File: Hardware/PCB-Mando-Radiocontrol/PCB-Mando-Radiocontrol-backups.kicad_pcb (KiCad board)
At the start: 2 copper layers, 132 x 66 mm, 25 parts, among them J1 USB 2.0 a UART TTL 6 pines CP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, J2 ALIMENTACION, SW1 SW_SPDT, SW2 SW_SPDT, SW3 SW_SPDT, U1 ATMEGA328P, U2 Nrf24l01, U3 AMS1117-3.3, U4 AMS1117-5.0, U5 COM-09032, U6 COM-09032, Y1 16MHZ

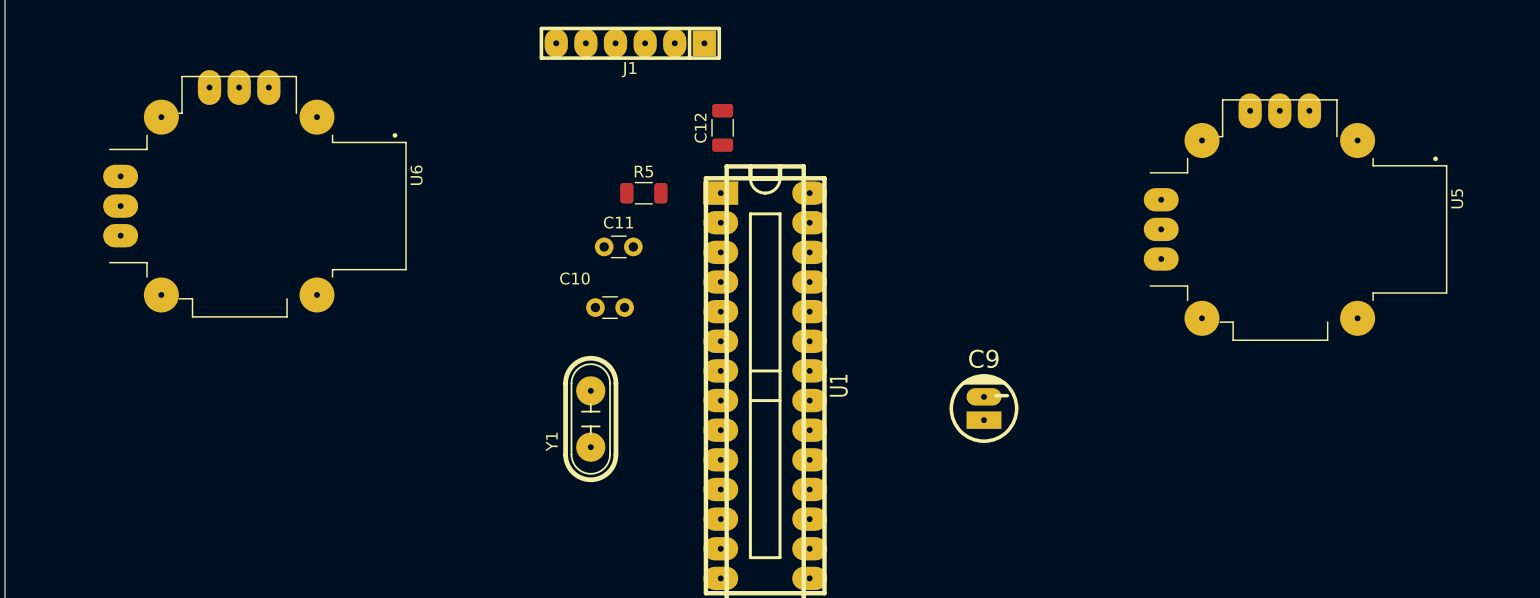
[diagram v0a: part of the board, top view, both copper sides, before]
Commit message: Reordenamiento de componentes
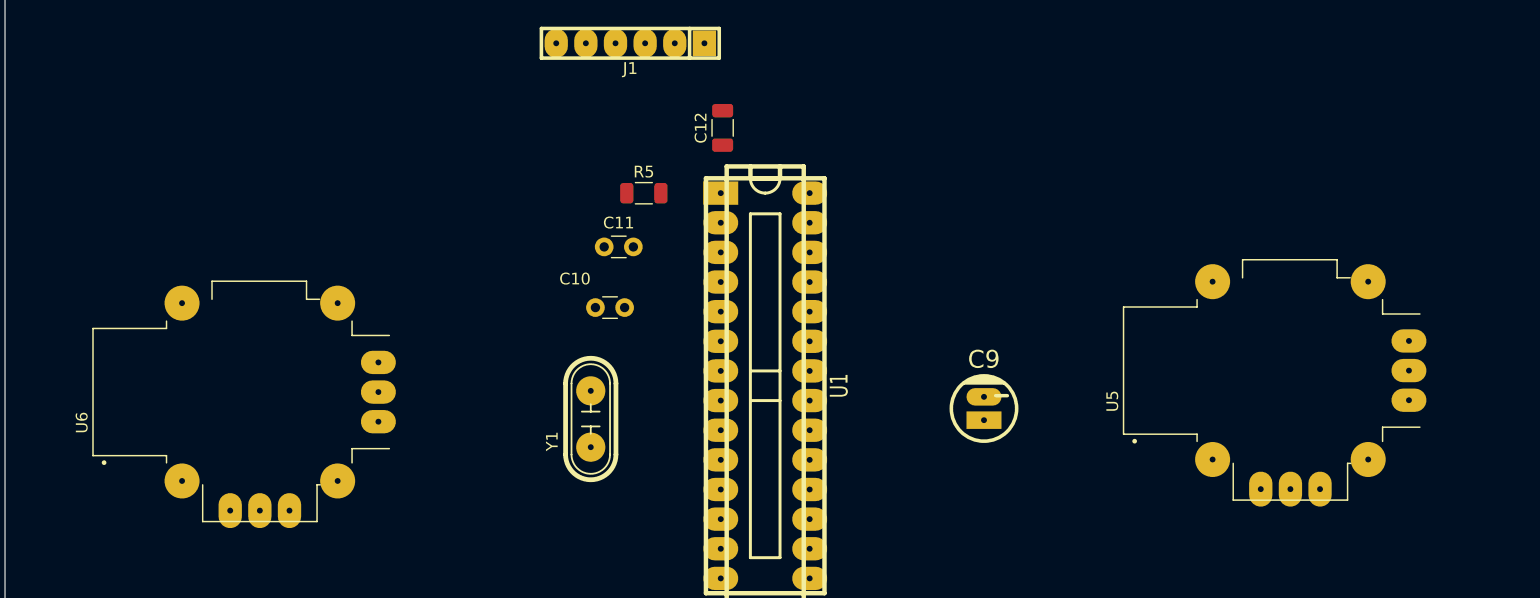
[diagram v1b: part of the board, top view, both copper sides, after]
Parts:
- moved U6 16.0 mm to (112.8, 98.8), turned to 90 degrees
- moved U5 12.1 mm to (201.2, 97.0), turned to 90 degrees
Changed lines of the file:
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@@
   )
   (footprint "PotStick:XDCR_COM-09032" (layer "F.Cu")
-    (at 111.068719 82.9 -90)
+    (at 112.84 98.84 90)
     (property "MANUFACTURER" "SparkFun Electronics")
     (property "MAXIMUM_PACKAGE_HEIGHT" "30.1mm")
@@
       (stroke (width 0.2) (type solid)) (fill none) (layer "F.Fab"))
     (dimension (type aligned) (layer "Edge.Cuts")
-      (pts (xy 117.736219 90.52) (xy 104.401219 90.52))
+      (pts (xy 106.1725 91.22) (xy 119.5075 91.22))
       (height -7.62)
-      (gr_text "13,3350 mm" (at 111.068719 96.99) (layer "Edge.Cuts")
+      (gr_text "13,3350 mm" (at 112.84 82.45) (layer "Edge.Cuts")
         (effects (font (size 1 1) (thickness 0.15)))
       )
@@
     )
     (dimension (type aligned) (layer "Edge.Cuts")
-      (pts (xy 113.608719 72.74) (xy 108.528719 72.74))
+      (pts (xy 110.3 109) (xy 115.38 109))
       (height 7.62)
-      (gr_text "5,0800 mm" (at 111.068719 63.97) (layer "Edge.Cuts")
+      (gr_text "5,0800 mm" (at 112.84 115.47) (layer "Edge.Cuts")
         (effects (font (size 1 1) (thickness 0.15)))
       )
@@
       (style (thickness 0.05) (arrow_length 1.27) (text_position_mode 0) (extension_height 0.58642) (extension_offset 0.5) keep_text_aligned)
     )
-    (pad "H1" thru_hole oval (at -2.54 10.16 270) (size 2 3) (drill 0.5) (layers "*.Cu" "*.Mask")
+    (pad "H1" thru_hole oval (at -2.54 10.16 90) (size 2 3) (drill 0.5) (layers "*.Cu" "*.Mask")
       (net 3 "+5V") (pinfunction "H+") (pintype "passive"))
-    (pad "H2" thru_hole oval (at 0 10.16 270) (size 2 3) (drill 0.5) (layers "*.Cu" "*.Mask")
+    (pad "H2" thru_hole oval (at 0 10.16 90) (size 2 3) (drill 0.5) (layers "*.Cu" "*.Mask")
       (net 27 "/PotIzqA") (pinfunction "H") (pintype "passive"))
-    (pad "H3" thru_hole oval (at 2.54 10.16 270) (size 2 3) (drill 0.5) (layers "*.Cu" "*.Mask")
+    (pad "H3" thru_hole oval (at 2.54 10.16 90) (size 2 3) (drill 0.5) (layers "*.Cu" "*.Mask")
       (net 2 "GND") (pinfunction "H-") (pintype "passive"))
-    (pad "S1" thru_hole circle (at -7.62 -6.6675 270) (size 3 3) (drill 0.5) (layers "*.Cu" "*.Mask")
+    (pad "S1" thru_hole circle (at -7.62 -6.6675 90) (size 3 3) (drill 0.5) (layers "*.Cu" "*.Mask")
       (net 2 "GND") (pinfunction "SHIELD") (pintype "passive"))
-    (pad "S2" thru_hole circle (at -7.62 6.6675 270) (size 3 3) (drill 0.5) (layers "*.Cu" "*.Mask")
+    (pad "S2" thru_hole circle (at -7.62 6.6675 90) (size 3 3) (drill 0.5) (layers "*.Cu" "*.Mask")
       (net 2 "GND") (pinfunction "SHIELD") (pintype "passive"))
-    (pad "S3" thru_hole circle (at 7.62 6.6675 270) (size 3 3) (drill 0.5) (layers "*.Cu" "*.Mask")
+    (pad "S3" thru_hole circle (at 7.62 6.6675 90) (size 3 3) (drill 0.5) (layers "*.Cu" "*.Mask")
       (net 2 "GND") (pinfunction "SHIELD") (pintype "passive"))
-    (pad "S4" thru_hole circle (at 7.62 -6.6675 270) (size 3 3) (drill 0.5) (layers "*.Cu" "*.Mask")
+    (pad "S4" thru_hole circle (at 7.62 -6.6675 90) (size 3 3) (drill 0.5) (layers "*.Cu" "*.Mask")
       (net 2 "GND") (pinfunction "SHIELD") (pintype "passive"))
-    (pad "V1" thru_hole oval (at -10.16 -2.54 270) (size 3 2) (drill 0.5) (layers "*.Cu" "*.Mask")
+    (pad "V1" thru_hole oval (at -10.16 -2.54 90) (size 3 2) (drill 0.5) (layers "*.Cu" "*.Mask")
       (net 3 "+5V") (pinfunction "V+") (pintype "passive"))
-    (pad "V2" thru_hole oval (at -10.16 0 270) (size 3 2) (drill 0.5) (layers "*.Cu" "*.Mask")
+    (pad "V2" thru_hole oval (at -10.16 0 90) (size 3 2) (drill 0.5) (layers "*.Cu" "*.Mask")
       (net 28 "/PotIzqB") (pinfunction "V") (pintype "passive"))
-    (pad "V3" thru_hole oval (at -10.16 2.54 270) (size 3 2) (drill 0.5) (layers "*.Cu" "*.Mask")
+    (pad "V3" thru_hole oval (at -10.16 2.54 90) (size 3 2) (drill 0.5) (layers "*.Cu" "*.Mask")
       (net 2 "GND") (pinfunction "V-") (pintype "passive"))
   )
@@
   )
   (footprint "PotStick:XDCR_COM-09032" (layer "F.Cu")
-    (at 200.25 84.9 -90)
+    (at 201.16 97 90)
     (property "MANUFACTURER" "SparkFun Electronics")
     (property "MAXIMUM_PACKAGE_HEIGHT" "30.1mm")
@@
       (stroke (width 0.2) (type solid)) (fill none) (layer "F.Fab"))
     (dimension (type aligned) (layer "Edge.Cuts")
-      (pts (xy 206.9175 92.52) (xy 193.5825 92.52))
+      (pts (xy 194.4925 89.38) (xy 207.8275 89.38))
       (height -7.62)
-      (gr_text "13,3350 mm" (at 200.25 98.99) (layer "Edge.Cuts")
+      (gr_text "13,3350 mm" (at 201.16 80.61) (layer "Edge.Cuts")
         (effects (font (size 1 1) (thickness 0.15)))
       )
@@
     )
     (dimension (type aligned) (layer "Edge.Cuts")
-      (pts (xy 202.79 74.74) (xy 197.71 74.74))
+      (pts (xy 198.62 107.16) (xy 203.7 107.16))
       (height 7.62)
-      (gr_text "5,0800 mm" (at 200.25 65.97) (layer "Edge.Cuts")
+      (gr_text "5,0800 mm" (at 201.16 113.63) (layer "Edge.Cuts")
         (effects (font (size 1 1) (thickness 0.15)))
       )
@@
       (style (thickness 0.05) (arrow_length 1.27) (text_position_mode 0) (extension_height 0.58642) (extension_offset 0.5) keep_text_aligned)
     )
-    (pad "H1" thru_hole oval (at -2.54 10.16 270) (size 2 3) (drill 0.5) (layers "*.Cu" "*.Mask")
+    (pad "H1" thru_hole oval (at -2.54 10.16 90) (size 2 3) (drill 0.5) (layers "*.Cu" "*.Mask")
       (net 3 "+5V") (pinfunction "H+") (pintype "passive"))
-    (pad "H2" thru_hole oval (at 0 10.16 270) (size 2 3) (drill 0.5) (layers "*.Cu" "*.Mask")
+    (pad "H2" thru_hole oval (at 0 10.16 90) (size 2 3) (drill 0.5) (layers "*.Cu" "*.Mask")
       (net 29 "/PotDerA") (pinfunction "H") (pintype "passive"))
-    (pad "H3" thru_hole oval (at 2.54 10.16 270) (size 2 3) (drill 0.5) (layers "*.Cu" "*.Mask")
+    (pad "H3" thru_hole oval (at 2.54 10.16 90) (size 2 3) (drill 0.5) (layers "*.Cu" "*.Mask")
       (net 2 "GND") (pinfunction "H-") (pintype "passive"))
-    (pad "S1" thru_hole circle (at -7.62 -6.6675 270) (size 3 3) (drill 0.5) (layers "*.Cu" "*.Mask")
+    (pad "S1" thru_hole circle (at -7.62 -6.6675 90) (size 3 3) (drill 0.5) (layers "*.Cu" "*.Mask")
       (net 2 "GND") (pinfunction "SHIELD") (pintype "passive"))
-    (pad "S2" thru_hole circle (at -7.62 6.6675 270) (size 3 3) (drill 0.5) (layers "*.Cu" "*.Mask")
+    (pad "S2" thru_hole circle (at -7.62 6.6675 90) (size 3 3) (drill 0.5) (layers "*.Cu" "*.Mask")
       (net 2 "GND") (pinfunction "SHIELD") (pintype "passive"))
-    (pad "S3" thru_hole circle (at 7.62 6.6675 270) (size 3 3) (drill 0.5) (layers "*.Cu" "*.Mask")
+    (pad "S3" thru_hole circle (at 7.62 6.6675 90) (size 3 3) (drill 0.5) (layers "*.Cu" "*.Mask")
       (net 2 "GND") (pinfunction "SHIELD") (pintype "passive"))
-    (pad "S4" thru_hole circle (at 7.62 -6.6675 270) (size 3 3) (drill 0.5) (layers "*.Cu" "*.Mask")
+    (pad "S4" thru_hole circle (at 7.62 -6.6675 90) (size 3 3) (drill 0.5) (layers "*.Cu" "*.Mask")
       (net 2 "GND") (pinfunction "SHIELD") (pintype "passive"))
-    (pad "V1" thru_hole oval (at -10.16 -2.54 270) (size 3 2) (drill 0.5) (layers "*.Cu" "*.Mask")
+    (pad "V1" thru_hole oval (at -10.16 -2.54 90) (size 3 2) (drill 0.5) (layers "*.Cu" "*.Mask")
       (net 3 "+5V") (pinfunction "V+") (pintype "passive"))
-    (pad "V2" thru_hole oval (at -10.16 0 270) (size 3 2) (drill 0.5) (layers "*.Cu" "*.Mask" "Eco2.User")
+    (pad "V2" thru_hole oval (at -10.16 0 90) (size 3 2) (drill 0.5) (layers "*.Cu" "*.Mask" "Eco2.User")
       (net 30 "/PotDerB") (pinfunction "V") (pintype "passive"))
-    (pad "V3" thru_hole oval (at -10.16 2.54 270) (size 3 2) (drill 0.5) (layers "*.Cu" "*.Mask")
+    (pad "V3" thru_hole oval (at -10.16 2.54 90) (size 3 2) (drill 0.5) (layers "*.Cu" "*.Mask")
       (net 2 "GND") (pinfunction "V-") (pintype "passive"))
   )
@@
   (gr_line (start 223 64) (end 91 64)
     (stroke (width 0.1) (type default)) (layer "Edge.Cuts"))
+  (dimension (type aligned) (layer "Edge.Cuts")
+    (pts (xy 115 109) (xy 115 130))
+    (height 0)
+    (gr_text "21,0000 mm" (at 113.85 119.5 90) (layer "Edge.Cuts")
+      (effects (font (size 1 1) (thickness 0.15)))
+    )
+    (format (prefix "") (suffix "") (units 3) (units_format 1) (precision 4))
+    (style (thickness 0.1) (arrow_length 1.27) (text_position_mode 0) (extension_height 0.58642) (extension_offset 0.5) keep_text_aligned)
+  )
 )

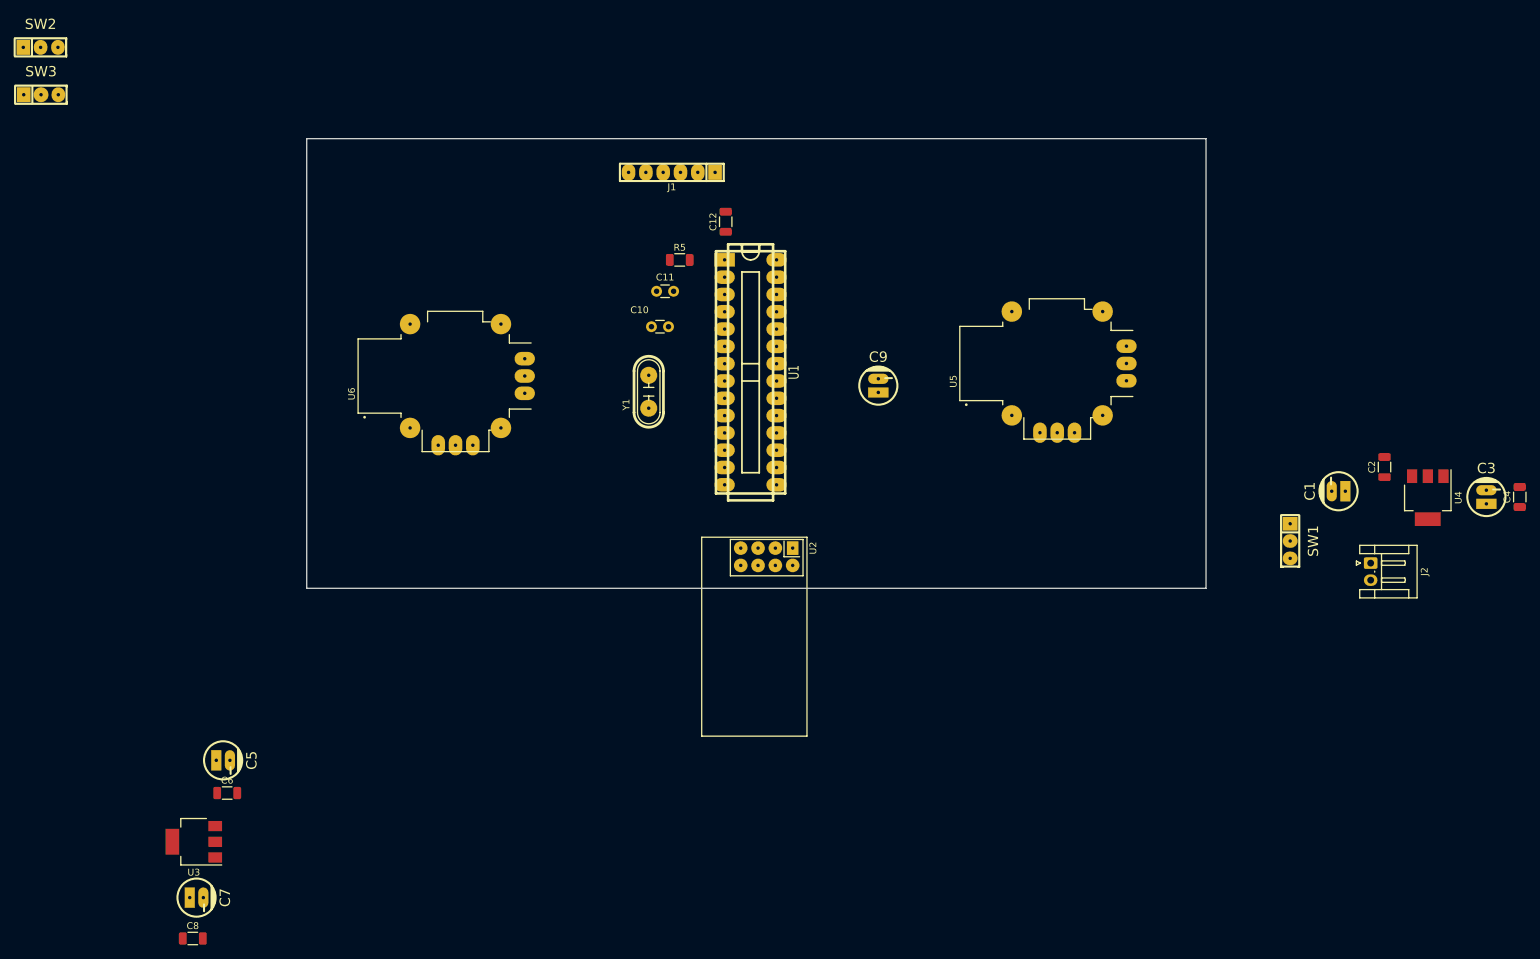
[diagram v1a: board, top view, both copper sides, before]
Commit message: PCB a medida con componentes a ordenar
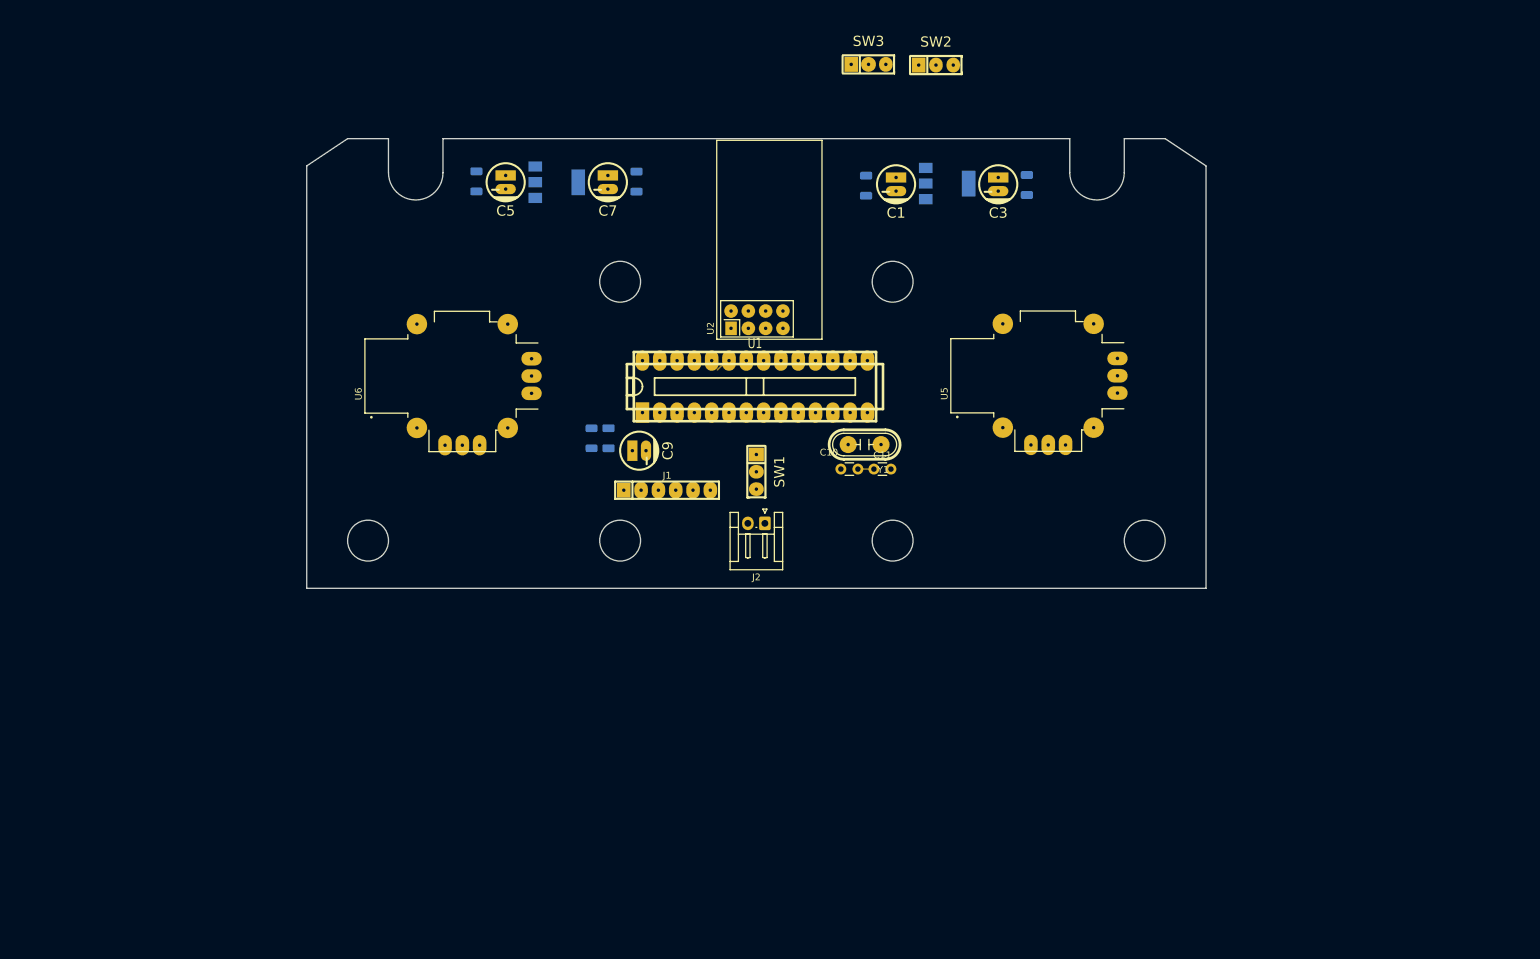
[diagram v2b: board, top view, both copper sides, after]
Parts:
- C12, C2, C4, C6, C8, R5, U3, U4: moved to B.Cu
- moved SW2 131.4 mm to (183.4, 53.2)
- moved C8 128.8 mm to (139.4, 70.3), turned to -90 degrees
- moved SW3 121.5 mm to (173.5, 53.1)
- moved C7 121.1 mm to (135.2, 70.4), turned to 180 degrees
- moved U3 110.5 mm to (127.7, 70.4), turned to 0 degrees
- moved C6 96.9 mm to (115.9, 70.3), turned to -90 degrees
- moved C5 94.4 mm to (120.2, 70.4), turned to 180 degrees
- moved J2 89.1 mm to (158.2, 120.5), turned to 180 degrees
- moved C2 86.6 mm to (173.1, 70.9), turned to -90 degrees
- moved C4 85.6 mm to (196.7, 70.8), turned to -90 degrees
- moved C3 85.1 mm to (192.5, 70.7), turned to 180 degrees
- moved U4 84.3 mm to (185.0, 70.6), turned to 0 degrees
- moved C1 79.0 mm to (177.5, 70.7), turned to 180 degrees
- moved SW1 79.0 mm to (157.0, 112.9)
- moved J1 46.7 mm to (143.9, 115.6), turned to 0 degrees
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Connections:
- J2 pad 1: /BAT -> GND
- J2 pad 2: GND -> /BAT
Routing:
- net GND: track 0.00 -> 2.35 mm
- net /PotIzqA: track 0.00 -> 1.16 mm
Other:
- outline, holes or cut-outs redrawn
